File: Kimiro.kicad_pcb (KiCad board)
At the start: 2 copper layers, 17.8 x 33 mm, 26 parts, among them J2 USB_C_Left, J3 Left, J4 Right, Q1 AO3407, U2 TP4054, U3 MS88FS3, U4 XC6220B331MR

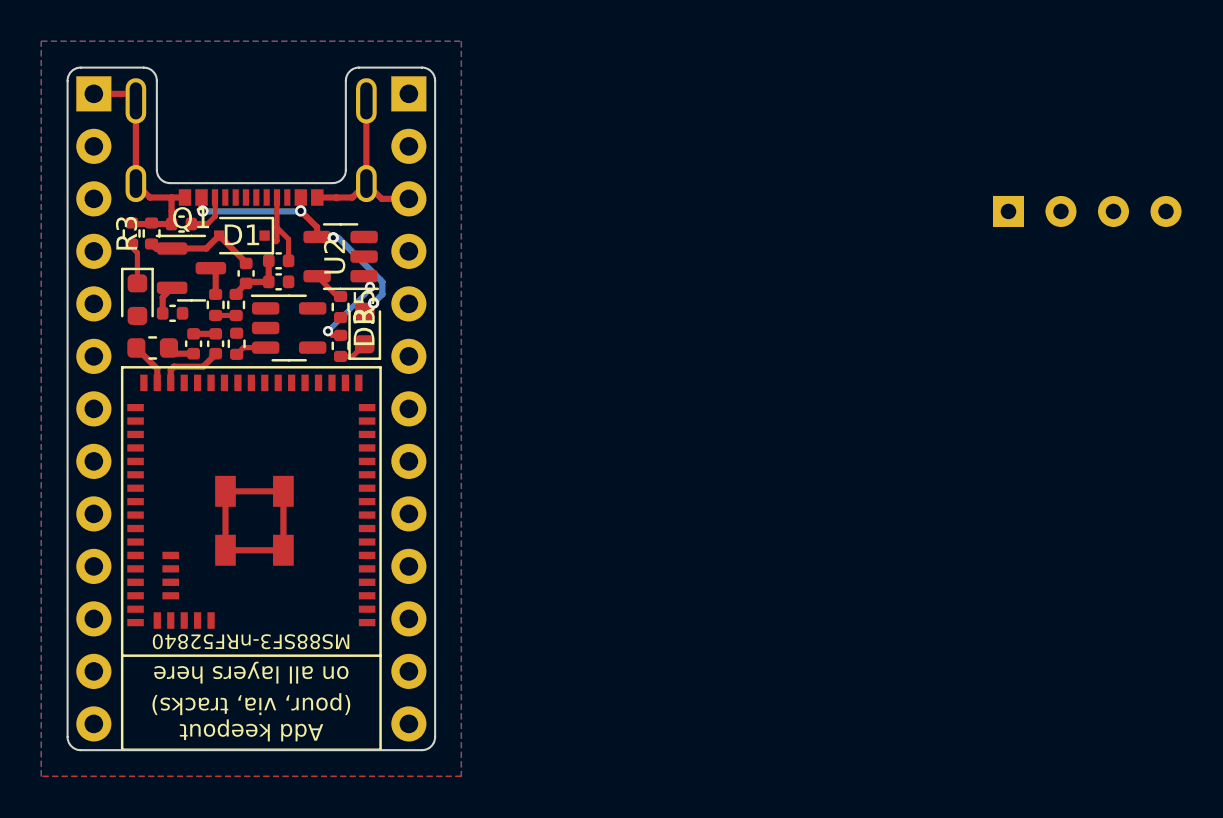
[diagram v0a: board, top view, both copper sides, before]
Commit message: v1.0 đã hoàn thành, cần tạo proto
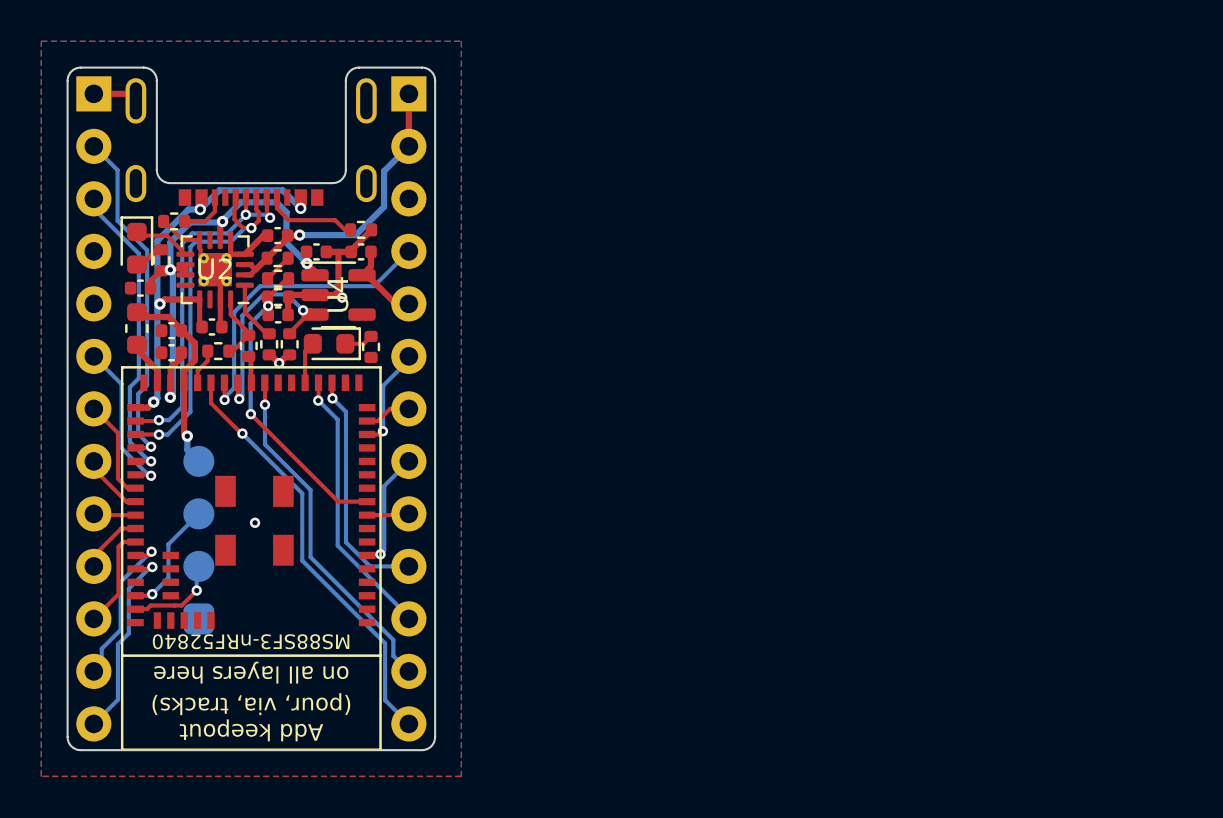
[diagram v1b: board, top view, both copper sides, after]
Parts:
- removed D3: RED, LED_SMD:LED_0603_1608Metric
- removed Q1: AO3407, Package_TO_SOT_SMD:SOT-23
- removed SWD1: SWD-STM32-4Pin, Sakura-library:Conn_1x04_P2.54mm
- added C2: 4.7uF, Capacitor_SMD:C_0402_1005Metric, F.Cu at (70.8, 43.7)
- added C3: 4.7uF, Capacitor_SMD:C_0402_1005Metric, F.Cu at (77.5, 41.1)
- added C4: 1nF, Capacitor_SMD:C_0402_1005Metric, F.Cu at (77.5, 45.0)
- added J1: Conn_01x04, Kimiro-library:Conn_1x04_P2.54mm, B.Cu at (73.7, 55.9)
- added R6: 10k, Resistor_SMD:R_0402_1005Metric, F.Cu at (71.9, 42.3)
- added R7: 2m, Resistor_SMD:R_0402_1005Metric, F.Cu at (77.5, 42.2)
- C1: value 10uF -> 1uF
- D1: value 1N5819 -> ORANGE; footprint Diode_SMD:D_SOD-323F -> LED_SMD:LED_0603_1608Metric
- J3, J4: footprint Sakura-library:Conn_1x13_P2.54mm -> Kimiro-library:Conn_1x13_P2.54mm
- R1, R2: footprint Capacitor_SMD:C_0402_1005Metric -> Resistor_SMD:R_0402_1005Metric
- R3: value 100K -> 10k
- R4: value 1K -> 10k
- R5: value RPROG -> 3.9k
- R8: value 820K -> 2m
- R9: value 2M -> 10k
- U2: value TP4054 -> BQ24075/9; footprint Package_TO_SOT_SMD:SOT-23-5 -> Package_DFN_QFN:VQFN-16-1EP_3x3mm_P0.5mm_EP1.6x1.6mm_ThermalVias
- moved R11 12.8 mm to (82.0, 46.5), turned to 90 degrees
- moved D2 9.51 mm to (80.0, 46.4), turned to 180 degrees
- moved R3 7.82 mm to (77.1, 46.4), turned to -90 degrees
- moved C5 6.60 mm to (79.3, 41.9), turned to 180 degrees
- moved U2 6.10 mm to (74.4, 42.8)
- moved R4 5.92 mm to (74.6, 46.7), turned to 0 degrees
- moved D1 5.12 mm to (70.7, 41.8), turned to -90 degrees
- moved R5 4.83 mm to (76.1, 46.5)
- moved R1 4.26 mm to (81.5, 40.9), turned to 0 degrees
- moved C6 4.24 mm to (81.5, 41.9)
- moved R8 3.28 mm to (77.5, 43.2), turned to 0 degrees
- moved C1 3.07 mm to (74.3, 45.6), turned to 0 degrees
- moved U4 2.87 mm to (80.4, 44.0)
- moved R10 2.57 mm to (78.1, 46.4)
- moved R9 2.07 mm to (77.5, 44.1), turned to 0 degrees
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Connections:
- C1 pad 1: GND -> VBUS
- C1 pad 2: VBUS -> GND
- D1 pad 1: VDDH -> Net-(D1-Pad1)
- D1 pad 2: VBUS -> Net-(D1-Pad2)
- J3 pad 10: unconnected-(J3-Pad10) -> 020
- J3 pad 11: unconnected-(J3-Pad11) -> 022
- J3 pad 12: unconnected-(J3-Pad12) -> 024
- J3 pad 13: unconnected-(J3-Pad13) -> 100
- J3 pad 2: unconnected-(J3-Pad2) -> 019
- J3 pad 3: unconnected-(J3-Pad3) -> 013
- J3 pad 6: unconnected-(J3-Pad6) -> 015
- J3 pad 7: unconnected-(J3-Pad7) -> 017
- J3 pad 8: unconnected-(J3-Pad8) -> 021
- J3 pad 9: unconnected-(J3-Pad9) -> 023
- J4 pad 10: unconnected-(J4-Pad10) -> 006
- J4 pad 11: unconnected-(J4-Pad11) -> 108
- J4 pad 12: unconnected-(J4-Pad12) -> 008
- J4 pad 13: unconnected-(J4-Pad13) -> 016
- J4 pad 2: unconnected-(J4-Pad2) -> VBAT
- J4 pad 6: unconnected-(J4-Pad6) -> 005
- J4 pad 7: unconnected-(J4-Pad7) -> 004
- J4 pad 8: unconnected-(J4-Pad8) -> 003
- J4 pad 9: unconnected-(J4-Pad9) -> 002
- R10 pad 1: VDDH -> POWER_PIN
- R10 pad 2: POWER_PIN -> GND
- R3 pad 1: VBUS -> Net-(R3-Pad1)
- R4 pad 1: Net-(D3-Pad1) -> CHARGE_CTRL_1
- R5 pad 1: Net-(R5-Pad1) -> Net-(R4-Pad2)
- R5 pad 2: GND -> CHARGE_CTRL_2
- R8 pad 1: VBAT -> Net-(R7-Pad2)
- U2 pad 1: Net-(R4-Pad2) -> Net-(R3-Pad1)
- U2 pad 2: GND -> VBAT
- U2 pad 4: VBUS -> GND
- U2 pad 5: Net-(R5-Pad1) -> GND
- U3 pad 10: unconnected-(U3-Pad10) -> BATTERY_PIN
- U3 pad 15: unconnected-(U3-Pad15) -> 005
- U3 pad 16: unconnected-(U3-Pad16) -> 004
- U3 pad 20: unconnected-(U3-Pad20) -> 006
- U3 pad 21: unconnected-(U3-Pad21) -> 108
- U3 pad 22: unconnected-(U3-Pad22) -> LED
- U3 pad 25: unconnected-(U3-Pad25) -> 008
- U3 pad 26: unconnected-(U3-Pad26) -> CHARGE_CTRL_2
- U3 pad 27: unconnected-(U3-Pad27) -> POWER_PIN
- U3 pad 29: CHARGE_CTRL_1 -> 016
- U3 pad 30: CHARGE_CTRL_2 -> CHARGE_CTRL_1
- U3 pad 34: unconnected-(U3-Pad34) -> GND
- U3 pad 38: unconnected-(U3-Pad38) -> 019
- U3 pad 39: unconnected-(U3-Pad39) -> 013
- U3 pad 40: unconnected-(U3-Pad40) -> 015
- U3 pad 41: unconnected-(U3-Pad41) -> 017
- U3 pad 42: unconnected-(U3-Pad42) -> 021
- U3 pad 43: unconnected-(U3-Pad43) -> 023
- U3 pad 44: unconnected-(U3-Pad44) -> 020
- U3 pad 45: unconnected-(U3-Pad45) -> 022
- U3 pad 46: unconnected-(U3-Pad46) -> 024
- U3 pad 47: unconnected-(U3-Pad47) -> 100
- U3 pad 6: unconnected-(U3-Pad6) -> 003
- U3 pad 9: unconnected-(U3-Pad9) -> 002
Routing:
- net 016: track 0.00 -> 20.5 mm, vias 0 -> 1
- net VDDH: track 4.60 -> 24.5 mm, vias 0 -> 4
- net D+: track 0.00 -> 18.2 mm, vias 0 -> 2
- net D-: track 0.00 -> 17.3 mm, vias 0 -> 3
- net 008: track 0.00 -> 16.9 mm, vias 0 -> 1
- net 019: track 0.00 -> 16.8 mm, vias 0 -> 1
- net GND: track 36.4 -> 21.4 mm, vias 0 -> 3
- net 013: track 0.00 -> 15.0 mm, vias 0 -> 1
- net RST: track 0.00 -> 14.9 mm, vias 0 -> 1
- net BATTERY_PIN: track 0.99 -> 15.4 mm, vias 0 -> 2
- net VBAT: track 1.36 -> 14.6 mm, vias 0 -> 1
- net 108: track 0.00 -> 13.3 mm, vias 0 -> 1
- net 006: track 0.00 -> 11.5 mm, vias 0 -> 1
- net 100: track 0.00 -> 9.66 mm, vias 0 -> 1
- net POWER_PIN: track 1.54 -> 10.9 mm, vias 0 -> 2
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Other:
- board text added: "*"
- board text added: "-"
- board text added: "002"
- board text added: "003"
- board text added: "004"
- board text added: "005"
- board text added: "006"
- board text added: "008"
- board text added: "013"
- board text added: "015"
- board text added: "016"
- board text added: "017"
- board text added: "019"
- board text added: "020"
- board text added: "021"
- board text added: "022"
- board text added: "023"
- board text added: "024"
- board text added: "100"
- board text added: "108"
- board text added: "AIN0"
- board text added: "AIN1"
- board text added: "AIN2"
- board text added: "AIN3"
- board text added: "B+"
- board text added: "CLK"
- board text added: "DIO"
- board text added: "GND"
- board text added: "KIMIRO"
- board text added: "RST"
- board text added: "VCC"
- board text added: "VDD"
- board text added: "v1.0"
- board text added: "{dblquote}*{dblquote} is low frequency I/O"

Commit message: cập nhật PCB
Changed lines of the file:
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@@
   (segment (start 70.041799 44.131199) (end 70.316617 43.856382) (width 0.3) (layer "F.Cu") (net 2))
   (segment (start 71.8592 45.7454) (end 71.75808 45.64428) (width 0.3) (layer "F.Cu") (net 2))
-  (segment (start 76.88795 41.148) (end 76.99 41.148) (width 0.3) (layer "F.Cu") (net 2))
   (segment (start 74.6974 43.650714) (end 74.6974 44.822286) (width 0.25) (layer "F.Cu") (net 2))
   (segment (start 71.8846 46.8122) (end 71.8846 46.854485) (width 0.3) (layer "F.Cu") (net 2))
-  (segment (start 76.127967 41.805931) (end 76.713739 41.22016) (width 0.3) (layer "F.Cu") (net 2))
+  (segment (start 76.127967 41.805931) (end 76.713739 41.22016) (width 0.25) (layer "F.Cu") (net 2))
   (segment (start 70.3606 43.7502) (end 70.3606 43.688) (width 0.3) (layer "F.Cu") (net 2))
   (segment (start 74.5724 42.924) (end 74.4474 42.799) (width 0.25) (layer "F.Cu") (net 2))
@@
   (arc (start 73.74692 41.992114) (mid 73.766474 42.09042) (end 73.82216 42.17376) (width 0.2) (layer "F.Cu") (net 2))
   (arc (start 79.259525 44.0182) (mid 79.266939 44.013245) (end 79.2652 44.0045) (width 0.3) (layer "F.Cu") (net 2))
-  (arc (start 76.127967 41.805931) (mid 75.858733 41.985828) (end 75.54115 42.049) (width 0.3) (layer "F.Cu") (net 2))
+  (arc (start 76.127967 41.805931) (mid 75.858733 41.985828) (end 75.54115 42.049) (width 0.25) (layer "F.Cu") (net 2))
   (arc (start 75.0974 42.149) (mid 75.17141 42.038234) (end 75.1974 41.907578) (width 0.25) (layer "F.Cu") (net 2))
   (arc (start 77.977 46.9158) (mid 77.952609 46.920651) (end 77.931932 46.934467) (width 0.3) (layer "F.Cu") (net 2))
@@
   (arc (start 81.055752 41.831447) (mid 81.035656 41.861523) (end 81.0286 41.897) (width 0.3) (layer "F.Cu") (net 2))
   (arc (start 71.999386 40.47348) (mid 71.986891 40.465131) (end 71.972153 40.4622) (width 0.2) (layer "F.Cu") (net 2))
-  (arc (start 76.88795 41.148) (mid 76.793667 41.166753) (end 76.713739 41.22016) (width 0.3) (layer "F.Cu") (net 2))
+  (arc (start 76.88795 41.148) (mid 76.793667 41.166753) (end 76.713739 41.22016) (width 0.25) (layer "F.Cu") (net 2))
   (arc (start 79.2652 44.0045) (mid 79.280374 44.014639) (end 79.298274 44.0182) (width 0.3) (layer "F.Cu") (net 2))
   (arc (start 72.601029 41.075123) (mid 72.918234 41.287073) (end 73.292403 41.3615) (width 0.2) (layer "F.Cu") (net 2))
@@
   (segment (start 75.55 48.935072) (end 75.55 48.269) (width 0.2) (layer "F.Cu") (net 15))
   (segment (start 75.6158 49.0474) (end 75.5829 49.0145) (width 0.2) (layer "F.Cu") (net 15))
+  (segment (start 79.2789 44.9682) (end 78.930999 44.9682) (width 0.2) (layer "F.Cu") (net 15))
   (segment (start 78.807998 45.091201) (end 78.0034 45.8958) (width 0.2) (layer "F.Cu") (net 15))
-  (segment (start 78.93086 44.764323) (end 78.702854 44.764323) (width 0.2) (layer "F.Cu") (net 15))
   (segment (start 79.10495 44.9682) (end 79.134737 44.9682) (width 0.2) (layer "F.Cu") (net 15))
+  (segment (start 78.930999 44.9682) (end 78.807998 45.091201) (width 0.2) (layer "F.Cu") (net 15))
   (via (at 78.702854 44.764323) (size 0.5) (drill 0.25) (layers "F.Cu" "B.Cu") (net 15))
   (via (at 75.6158 49.0474) (size 0.5) (drill 0.25) (layers "F.Cu" "B.Cu") (net 15))
   (arc (start 79.176961 44.866261) (mid 79.189905 44.931337) (end 79.134737 44.9682) (width 0.2) (layer "F.Cu") (net 15))
-  (arc (start 79.176961 44.866261) (mid 79.064049 44.790815) (end 78.93086 44.764323) (width 0.2) (layer "F.Cu") (net 15))
   (arc (start 75.55 48.935072) (mid 75.55855 48.978058) (end 75.5829 49.0145) (width 0.2) (layer "F.Cu") (net 15))
   (arc (start 79.10495 44.9682) (mid 78.94424 45.000166) (end 78.807998 45.091201) (width 0.2) (layer "F.Cu") (net 15))
@@
   (segment (start 71.384817 45.08588) (end 71.712222 45.08588) (width 0.3) (layer "F.Cu") (net 44))
   (segment (start 72.95 47.9845) (end 72.95 48.5535) (width 0.3) (layer "F.Cu") (net 44))
+  (segment (start 73.47028 46.766957) (end 73.470279 46.535966) (width 0.3) (layer "F.Cu") (net 44))
   (segment (start 73.0256 50.7752) (end 73.1012 50.8508) (width 0.3) (layer "F.Cu") (net 44))
   (segment (start 70.830562 44.8563) (end 70.6628 44.8563) (width 0.3) (layer "F.Cu") (net 44))
-  (segment (start 72.548265 45.43218) (end 73.178412 46.062327) (width 0.3) (layer "F.Cu") (net 44))
-  (segment (start 73.210139 47.439859) (end 73.151171 47.498828) (width 0.3) (layer "F.Cu") (net 44))
+  (segment (start 73.47028 46.811826) (end 73.47028 46.982253) (width 0.3) (layer "F.Cu") (net 44))
+  (segment (start 72.548265 45.43218) (end 73.341746 46.225661) (width 0.3) (layer "F.Cu") (net 44))
+  (segment (start 73.330654 47.319342) (end 73.151171 47.498828) (width 0.3) (layer "F.Cu") (net 44))
   (segment (start 73.47028 46.811826) (end 73.47028 46.766957) (width 0.3) (layer "F.Cu") (net 44))
   (segment (start 72.95 50.592685) (end 72.95 48.5535) (width 0.3) (layer "F.Cu") (net 44))
   (via (at 73.1012 50.8508) (size 0.55) (drill 0.25) (layers "F.Cu" "B.Cu") (net 44))
   (arc (start 73.151171 47.498828) (mid 73.002282 47.721656) (end 72.95 47.9845) (width 0.3) (layer "F.Cu") (net 44))
-  (arc (start 73.178412 46.062327) (mid 73.394425 46.385614) (end 73.47028 46.766957) (width 0.3) (layer "F.Cu") (net 44))
+  (arc (start 73.341746 46.225661) (mid 73.436874 46.36803) (end 73.470279 46.535966) (width 0.3) (layer "F.Cu") (net 44))
   (arc (start 71.10769 44.97109) (mid 71.234837 45.056047) (end 71.384817 45.08588) (width 0.3) (layer "F.Cu") (net 44))
   (arc (start 71.10769 44.97109) (mid 70.980542 44.886132) (end 70.830562 44.8563) (width 0.3) (layer "F.Cu") (net 44))
   (arc (start 72.548265 45.43218) (mid 72.164685 45.17588) (end 71.712222 45.08588) (width 0.3) (layer "F.Cu") (net 44))
-  (arc (start 73.47028 46.811826) (mid 73.402671 47.151715) (end 73.210139 47.439859) (width 0.3) (layer "F.Cu") (net 44))
+  (arc (start 73.47028 46.982253) (mid 73.433992 47.164684) (end 73.330654 47.319342) (width 0.3) (layer "F.Cu") (net 44))
   (arc (start 72.95 50.592685) (mid 72.969647 50.691461) (end 73.0256 50.7752) (width 0.3) (layer "F.Cu") (net 44))
   (segment (start 73.334686 51.744686) (end 73.66 52.07) (width 0.3) (layer "B.Cu") (net 44))

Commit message: 19:28 22/03/2022
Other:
- outline, holes or cut-outs redrawn
